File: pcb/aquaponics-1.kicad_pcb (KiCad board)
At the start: 2 copper layers, 67.3 x 63.5 mm, 17 parts, among them J1 5V Power Source, J2 Screw_Terminal_01x02, J3 Water Level Sensor, J4 Rain Sensor, J5 Conn_01x02_Female, M1 Growbed Pump, M2 Overflow Pump, M3 Fish Feeder, Q1 TIP120, Q2 TIP120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

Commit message: 1st draft
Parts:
- removed J3: Water Level Sensor, Connector_PinHeader_1.00mm:PinHeader_1x03_P1.00mm_Vertical
- removed J4: Rain Sensor, Connector_PinHeader_1.00mm:PinHeader_1x03_P1.00mm_Vertical
- removed M1: Growbed Pump, Connector_PinHeader_1.00mm:PinHeader_1x02_P1.00mm_Vertical
- removed M2: Overflow Pump, Connector_PinHeader_1.00mm:PinHeader_1x02_P1.00mm_Vertical
- removed M3: Fish Feeder, Connector_PinHeader_1.00mm:PinHeader_1x02_P1.00mm_Vertical
- removed R1: Light Sensor, Connector_PinHeader_1.00mm:PinHeader_1x02_P1.00mm_Vertical
- added Feed: Fish Feeder, Connector_PinHeader_1.00mm:PinHeader_1x02_P1.00mm_Vertical, F.Cu at (64.5, 45.7)
- added Level: Water Level Sensor, Connector_PinHeader_1.00mm:PinHeader_1x03_P1.00mm_Vertical, F.Cu at (22.2, 47.0)
- added Light: Light Sensor, Connector_PinHeader_1.00mm:PinHeader_1x02_P1.00mm_Vertical, F.Cu at (23.5, 55.9)
- added Overflow: Overflow Pump, Connector_PinHeader_1.00mm:PinHeader_1x02_P1.00mm_Vertical, F.Cu at (64.5, 34.3)
- added Pump: Growbed Pump, Connector_PinHeader_1.00mm:PinHeader_1x02_P1.00mm_Vertical, F.Cu at (64.5, 57.1)
- added R6: 10k, Resistor_THT:R_Axial_DIN0204_L3.6mm_D1.6mm_P5.08mm_Horizontal, F.Cu at (21.6, 38.1)
- added Rain: Rain Sensor, Connector_PinHeader_1.00mm:PinHeader_1x03_P1.00mm_Vertical, F.Cu at (22.2, 43.2)
- added Temp: DHT11, Sensor:Aosong_DHT11_5.5x12.0_P2.54mm, F.Cu at (23.5, 19.7)
- J2: footprint TerminalBlock_Phoenix:TerminalBlock_Phoenix_MPT-0,5-2-2.54_1x02_P2.54mm_Horizontal -> TerminalBlock_Phoenix:TerminalBlock_Phoenix_PT-1,5-2-5.0-H_1x02_P5.00mm_Horizontal
- moved R3 54.5 mm to (22.2, 51.4)
- moved J5 46.4 mm to (65.4, 74.4), turned to 90 degrees
- moved J2 38.6 mm to (62.2, 20.3), turned to 180 degrees
- moved Q2 32.8 mm to (57.1, 36.8), turned to 90 degrees
- moved R2 31.9 mm to (48.9, 36.8), turned to 0 degrees
- moved J1 25.5 mm to (50.2, 74.3), turned to 90 degrees
- moved U1 21.7 mm to (43.2, 66.0), turned to 180 degrees
- moved Q3 16.5 mm to (57.1, 48.3), turned to 90 degrees
- moved R5 15.5 mm to (48.9, 48.3), turned to 0 degrees
- moved Q1 7.41 mm to (57.1, 59.7), turned to 90 degrees
- moved R4 6.63 mm to (48.9, 59.7), turned to 0 degrees
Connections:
- net Net-(J1-Pad1) renamed +5V
- J1 pad 2: (no net) -> Net-(J1-Pad2)
- J5 pad 2: (no net) -> Net-(J5-Pad2)
- U1 pad 1: (no net) -> Net-(U1-Pad1)
- U1 pad 11: (no net) -> Net-(U1-Pad11)
- U1 pad 12: (no net) -> Net-(U1-Pad12)
- U1 pad 13: (no net) -> Net-(U1-Pad13)
- U1 pad 14: (no net) -> Net-(U1-Pad14)
- U1 pad 15: (no net) -> Net-(U1-Pad15)
- U1 pad 17: (no net) -> +3V3
- U1 pad 18: (no net) -> Net-(U1-Pad18)
- U1 pad 19: Net-(R1-Pad1) -> Net-(R6-Pad1)
- U1 pad 2: (no net) -> Net-(U1-Pad2)
- U1 pad 22: (no net) -> Net-(R1-Pad1)
- U1 pad 23: (no net) -> Net-(U1-Pad23)
- U1 pad 24: (no net) -> Net-(U1-Pad24)
- U1 pad 25: (no net) -> Net-(U1-Pad25)
- U1 pad 26: (no net) -> Net-(U1-Pad26)
- U1 pad 28: (no net) -> Net-(U1-Pad28)
- U1 pad 29: (no net) -> Net-(U1-Pad29)
- U1 pad 3: (no net) -> Net-(U1-Pad3)
- U1 pad 30: (no net) -> Net-(U1-Pad30)
- U1 pad 8: (no net) -> Net-(U1-Pad8)
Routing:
- net Net-(U1-Pad9): track 43.8 -> 0.00 mm
- net +5V: track 29.4 -> 67.2 mm
- net Net-(J4-Pad3): track 38.7 -> 4.77 mm
- net Net-(U1-Pad10): track 33.6 -> 0.00 mm
- net Net-(R6-Pad1): track 0.00 -> 26.5 mm
- net +3V3: track 0.00 -> 20.5 mm
- net Net-(J2-Pad1): track 80.1 -> 95.6 mm
- net Net-(R2-Pad1): track 29.2 -> 16.3 mm
- net Net-(R5-Pad1): track 19.0 -> 7.82 mm
- net Net-(U1-Pad16): track 6.40 -> 0.00 mm
- net GND: track 129.6 -> 123.3 mm
- net Net-(J3-Pad3): track 0.00 -> 5.35 mm
- net Net-(Q1-Pad1): track 9.52 -> 6.35 mm
- net Net-(M3-Pad2): track 9.00 -> 6.35 mm
- net Net-(Q3-Pad1): track 8.26 -> 6.35 mm
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- removed copper zone on B.Cu, net GND
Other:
- board size 67.3 x 63.5 mm -> 52.1 x 63.5 mm
- board text removed: "Arduino Nano"

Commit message: Update PCB'
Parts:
- J3: renamed from Level; footprint Connector_PinHeader_1.00mm:PinHeader_1x03_P1.00mm_Vertical -> Connector_PinHeader_2.54mm:PinHeader_1x03_P2.54mm_Vertical
- J4: renamed from Rain; footprint Connector_PinHeader_1.00mm:PinHeader_1x03_P1.00mm_Vertical -> Connector_PinHeader_2.54mm:PinHeader_1x03_P2.54mm_Vertical
- M1: renamed from Pump; footprint Connector_PinHeader_1.00mm:PinHeader_1x02_P1.00mm_Vertical -> Connector_PinHeader_2.54mm:PinHeader_1x02_P2.54mm_Vertical
- M2: renamed from Overflow; footprint Connector_PinHeader_1.00mm:PinHeader_1x02_P1.00mm_Vertical -> Connector_PinHeader_2.54mm:PinHeader_1x02_P2.54mm_Vertical
- M3: renamed from Feed; footprint Connector_PinHeader_1.00mm:PinHeader_1x02_P1.00mm_Vertical -> Connector_PinHeader_2.54mm:PinHeader_1x02_P2.54mm_Vertical
- R1: renamed from Light; footprint Connector_PinHeader_1.00mm:PinHeader_1x02_P1.00mm_Vertical -> Connector_PinHeader_2.54mm:PinHeader_1x02_P2.54mm_Vertical
- R6: footprint Resistor_THT:R_Axial_DIN0204_L3.6mm_D1.6mm_P5.08mm_Horizontal -> Resistor_THT:R_Axial_DIN0204_L3.6mm_D1.6mm_P1.90mm_Vertical
- moved R1 14.7 mm to (22.2, 70.5), turned to 0 degrees
- moved R3 13.3 mm to (22.2, 64.8), turned to 90 degrees
- moved J3 11.4 mm to (22.2, 58.4), turned to 180 degrees
- moved U2 5.24 mm to (22.2, 24.8), turned to 180 degrees
- moved J4 5.08 mm to (22.2, 48.3), turned to 180 degrees
- renumbered Temp to U2
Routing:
- net Net-(R1-Pad1): track 12.0 -> 38.2 mm
- net GND: track 123.3 -> 131.9 mm
- net Net-(J3-Pad3): track 5.35 -> 12.5 mm
- net Net-(R6-Pad1): track 26.5 -> 23.3 mm
- net +3V3: track 20.5 -> 18.3 mm
- net Net-(J4-Pad3): track 4.77 -> 6.77 mm
- net +5V: track 67.2 -> 68.1 mm

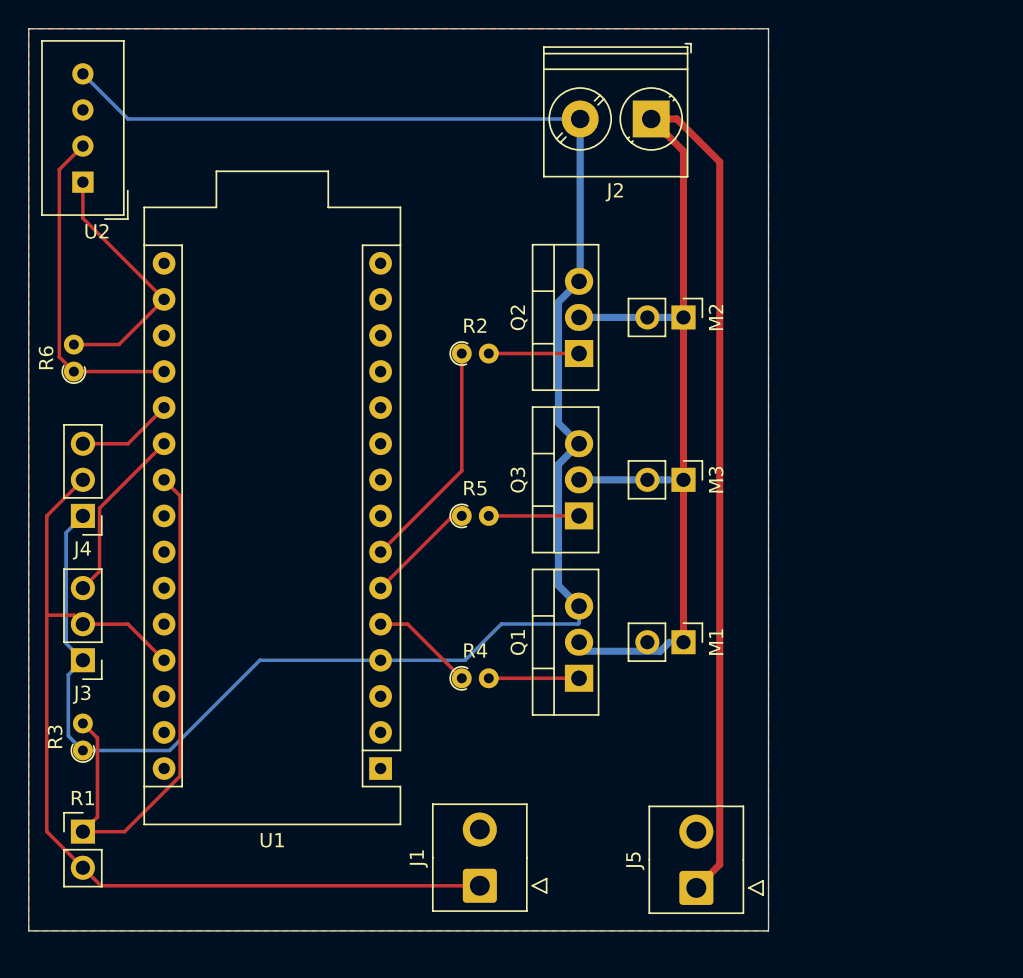
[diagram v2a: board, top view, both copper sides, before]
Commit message: Temp sensor to use 5V power
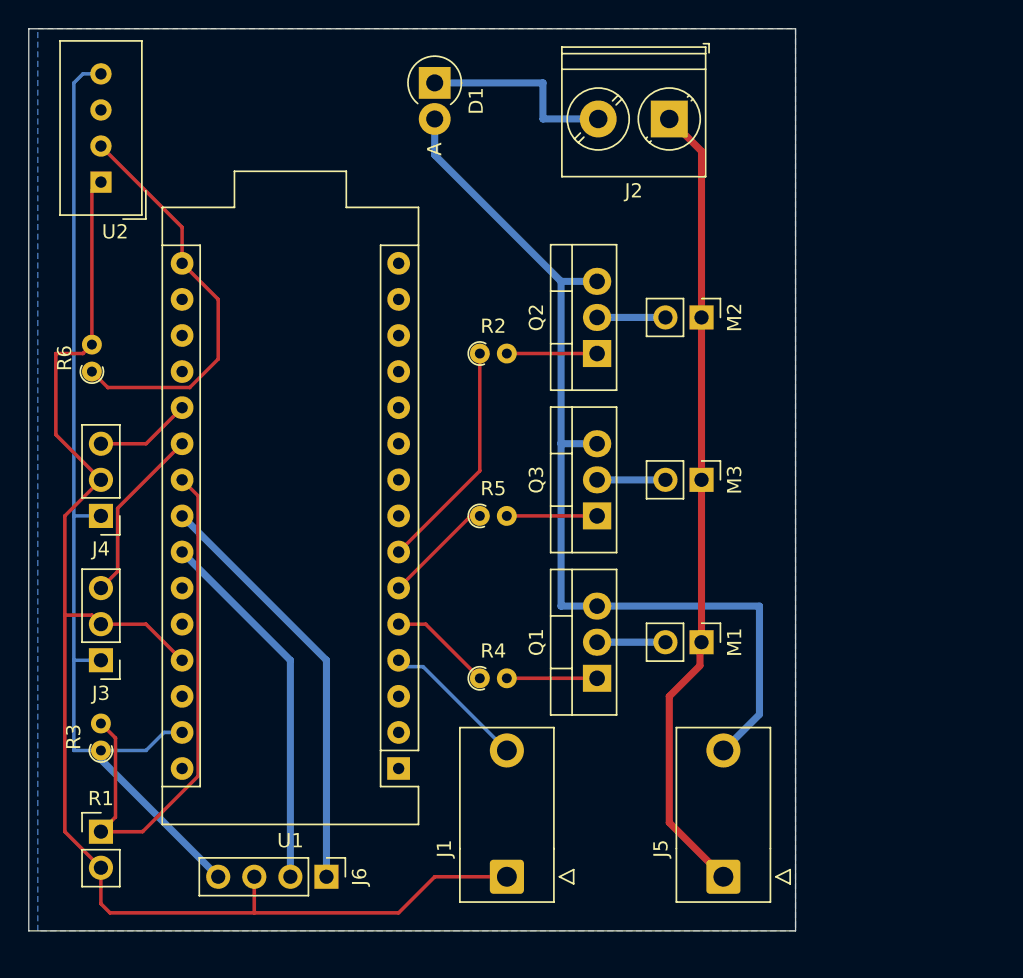
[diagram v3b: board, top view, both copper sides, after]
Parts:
- added D1: DIODE, Diode_THT:D_DO-15_P2.54mm_Vertical_AnodeUp, F.Cu at (47.0, 17.8)
- added J6: Conn_01x04_Female, Connector_PinHeader_2.54mm:PinHeader_1x04_P2.54mm_Vertical, F.Cu at (39.4, 73.7)
- J1, J5: footprint Connector_TE-Connectivity:TE_826576-2_1x02_P3.96mm_Vertical -> aquaponics-1:VP-TE_826576-2_1x02_P3.96mm_Vertical
- R3: value 330 -> 10k
- moved J5 2.06 mm to (67.3, 73.7)
- moved J1 2.01 mm to (52.1, 73.7)
- moved J2 1.27 mm to (63.5, 20.3)
- moved Q1 1.27 mm to (58.4, 59.7)
- moved Q2 1.27 mm to (58.4, 36.8)
- moved Q3 1.27 mm to (58.4, 48.3)
- moved U1 1.27 mm to (44.5, 66.0)
- moved J3 1.27 mm to (23.5, 58.4)
- moved J4 1.27 mm to (23.5, 48.3)
- moved R1 1.27 mm to (23.5, 70.5)
- moved R3 1.27 mm to (23.5, 64.8)
- moved R6 1.27 mm to (22.9, 38.1)
- moved U2 1.27 mm to (23.5, 24.8)
- moved M1 1.27 mm to (65.8, 57.1)
- moved M2 1.27 mm to (65.8, 34.3)
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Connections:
- J1 pad 2: Net-(J1-Pad2) -> GND1
- J2 pad 2: GND -> Net-(D1-Pad1)
- J3 pad 1: GND -> GND1
- J4 pad 1: GND -> GND1
- J5 pad 2: Net-(J5-Pad2) -> GND
- R3 pad 1: GND -> GND1
- R6 pad 2: +3V3 -> +5V
- U1 pad 16: Net-(U1-Pad16) -> Net-(R6-Pad1)
- U1 pad 17: +3V3 -> Net-(U1-Pad17)
- U1 pad 19: Net-(R6-Pad1) -> Net-(U1-Pad19)
- U1 pad 29: Net-(U1-Pad29) -> GND1
- U1 pad 4: GND -> GND1
- U2 pad 1: +3V3 -> +5V
- U2 pad 4: GND -> GND1
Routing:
- net GND1: track 0.00 -> 83.9 mm
- net GND: track 131.9 -> 68.2 mm
- net Net-(J2-Pad1): track 95.6 -> 56.8 mm
- net +5V: track 68.1 -> 99.0 mm
- net Net-(J6-Pad1): track 0.00 -> 29.6 mm
- net Net-(J6-Pad2): track 0.00 -> 26.0 mm
- net +3V3: track 18.3 -> 0.00 mm
- net Net-(D1-Pad1): track 0.00 -> 14.0 mm
- net Net-(R6-Pad1): track 23.3 -> 28.6 mm
- net Net-(M2-Pad2): track 7.89 -> 4.81 mm
- net Net-(M1-Pad2): track 7.25 -> 4.81 mm
- net Net-(M3-Pad2): track 6.35 -> 4.81 mm
- added copper zone on B.Cu, net GND
- removed copper zone on F.Cu, net GND
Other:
- board size 52.1 x 63.5 mm -> 54 x 63.5 mm
